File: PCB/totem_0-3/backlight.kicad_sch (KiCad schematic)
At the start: 40 parts

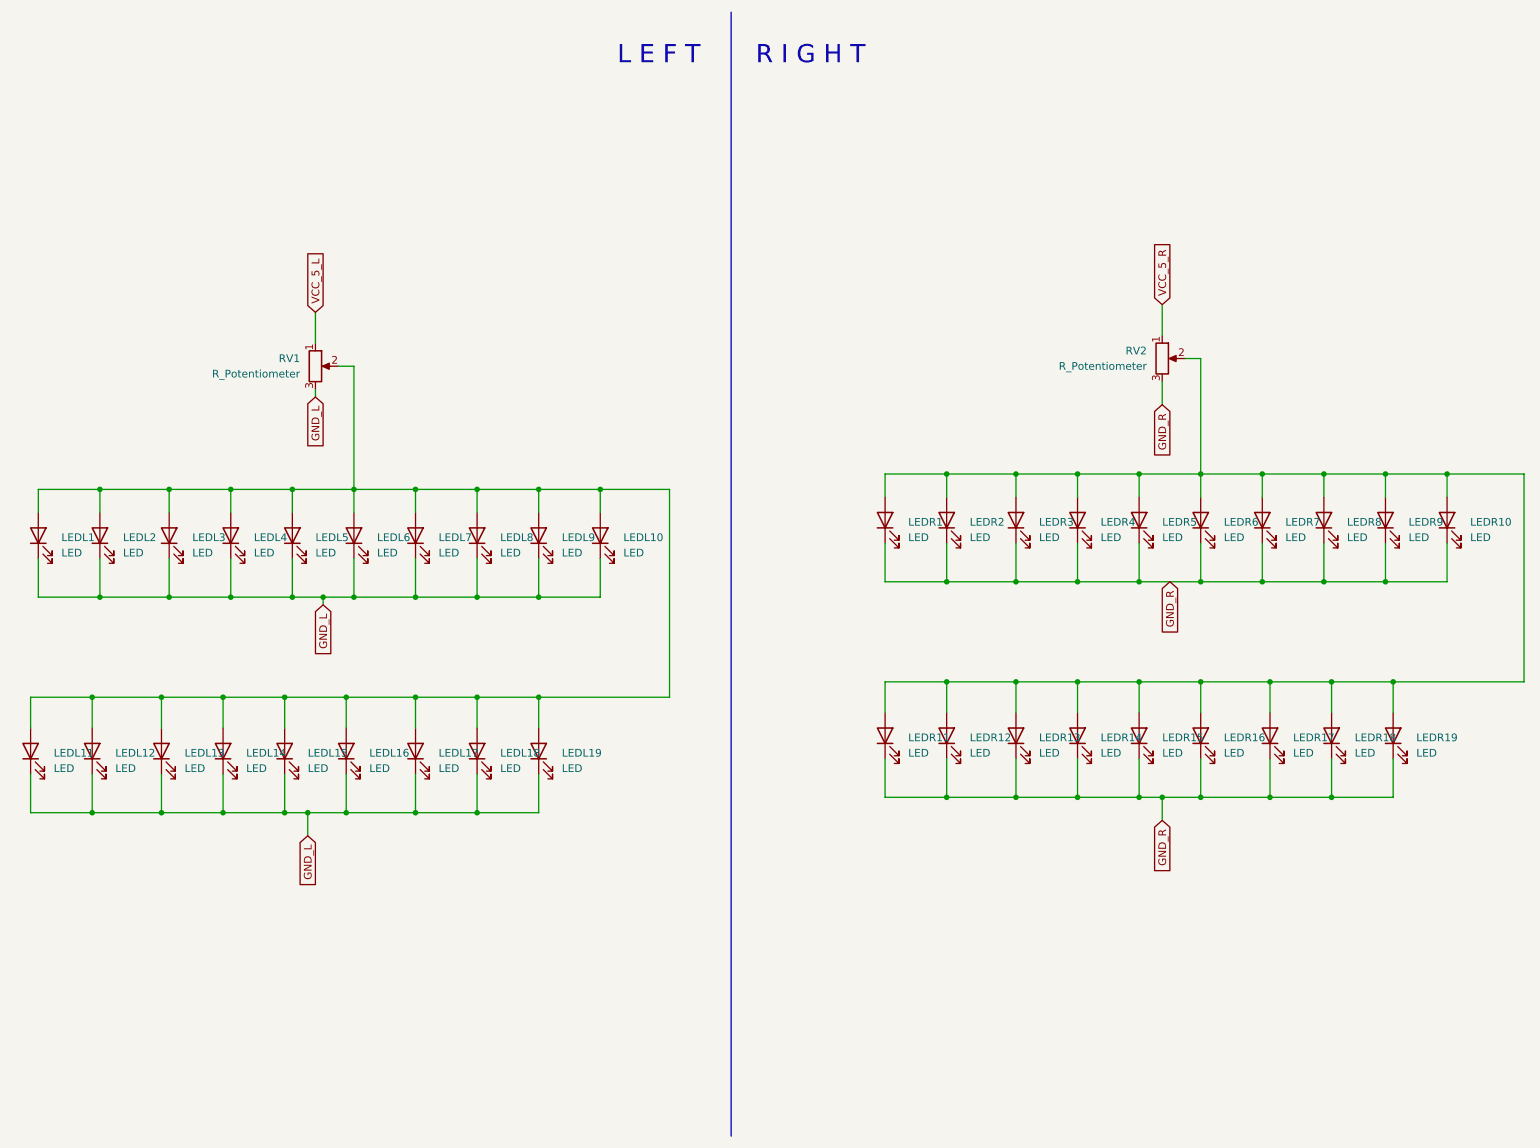
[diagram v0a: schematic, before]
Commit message: updated backlight shematics with new leds, default led uses reversed pin number assigns, aka : leds get mounted backwards by pick and place, what a tragedy
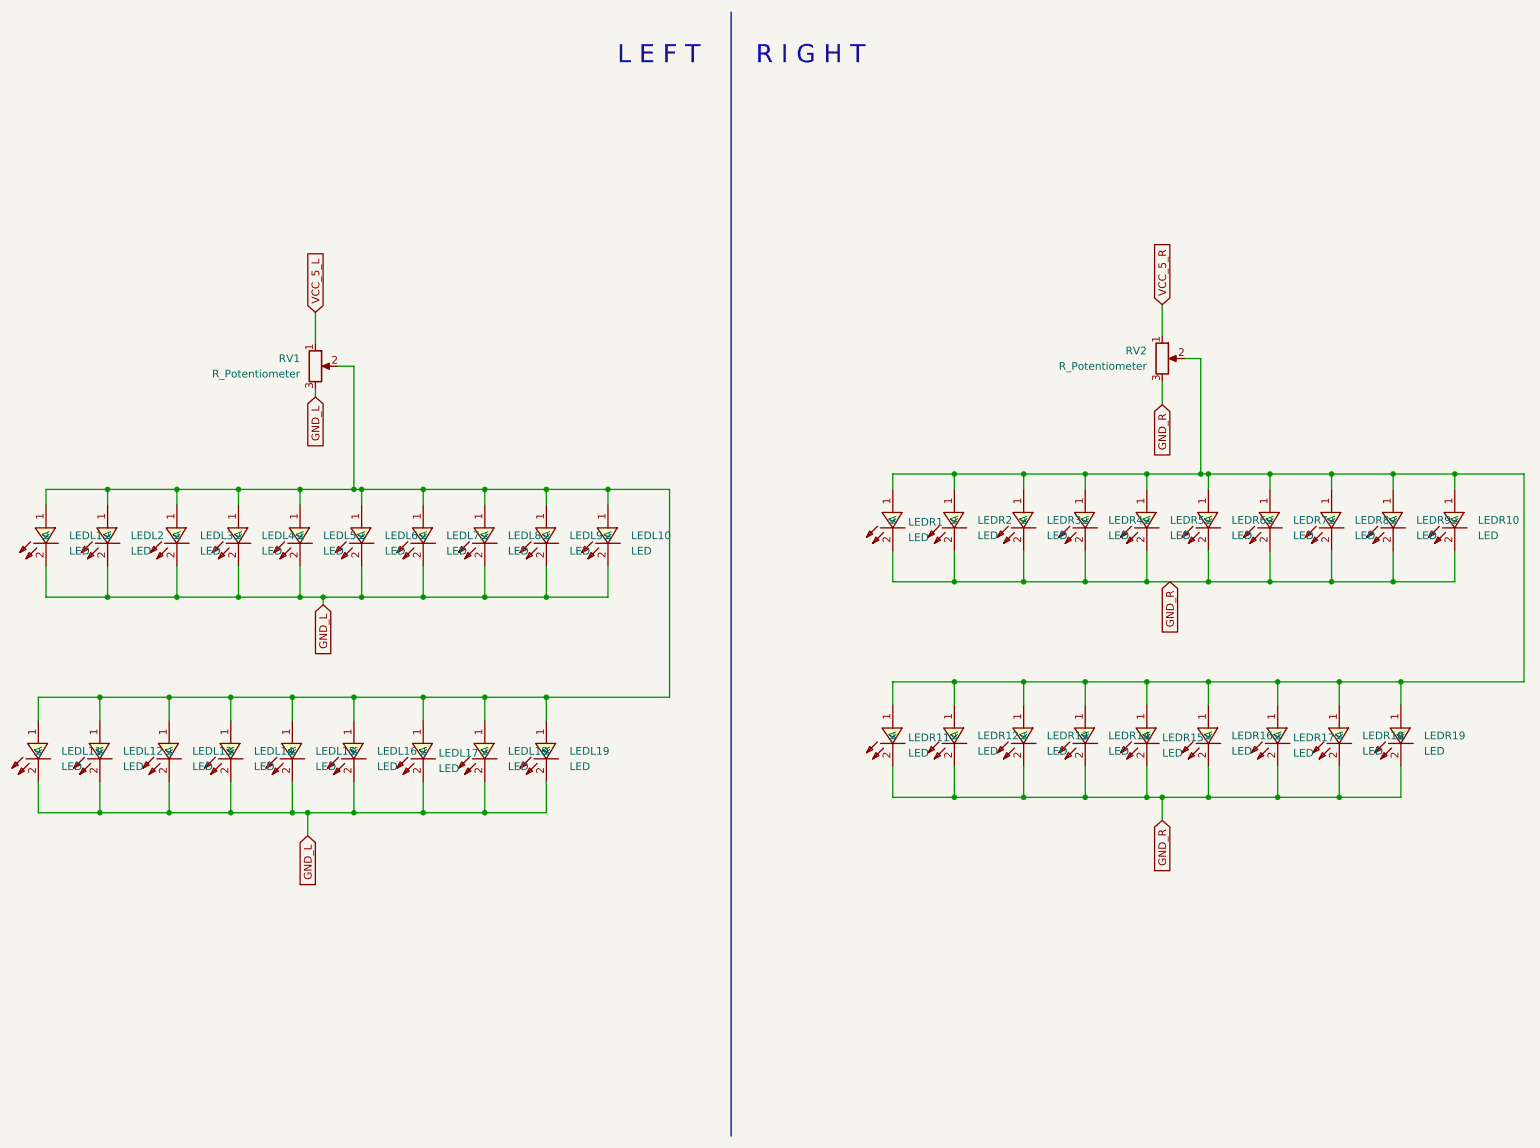
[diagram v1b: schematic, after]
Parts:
- LEDL1, LEDL10, LEDL11, LEDL12, LEDL13, LEDL14, LEDL15, LEDL16, LEDL17, LEDL18, LEDL19, LEDL2, LEDL3, LEDL4, LEDL5, LEDL6, LEDL7, LEDL8, LEDL9, LEDR1, LEDR10, LEDR11, LEDR12, LEDR13, LEDR14, LEDR15, LEDR16, LEDR17, LEDR18, LEDR19, LEDR2, LEDR3, LEDR4, LEDR5, LEDR6, LEDR7, LEDR8, LEDR9: symbol Device:LED -> Totem_lib:0603Whitelight_C2290; LCSC Part (none) -> C2290
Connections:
- net GND_L: now also LEDL1.2 (K), LEDL10.2 (K), LEDL11.2 (K), LEDL12.2 (K), LEDL13.2 (K), LEDL14.2 (K), LEDL15.2 (K), LEDL16.2 (K), LEDL17.2 (K), LEDL18.2 (K), LEDL19.2 (K), LEDL2.2 (K), LEDL3.2 (K), LEDL4.2 (K), LEDL5.2 (K), LEDL6.2 (K), LEDL7.2 (K), LEDL8.2 (K), LEDL9.2 (K); no longer LEDL1.1 (K), LEDL10.1 (K), LEDL11.1 (K), LEDL12.1 (K), LEDL13.1 (K), LEDL14.1 (K), LEDL15.1 (K), LEDL16.1 (K), LEDL17.1 (K), LEDL18.1 (K), LEDL19.1 (K), LEDL2.1 (K), LEDL3.1 (K), LEDL4.1 (K), LEDL5.1 (K), LEDL6.1 (K), LEDL7.1 (K), LEDL8.1 (K), LEDL9.1 (K)
- net GND_R: now also LEDR1.2 (K), LEDR10.2 (K), LEDR11.2 (K), LEDR12.2 (K), LEDR13.2 (K), LEDR14.2 (K), LEDR15.2 (K), LEDR16.2 (K), LEDR17.2 (K), LEDR18.2 (K), LEDR19.2 (K), LEDR2.2 (K), LEDR3.2 (K), LEDR4.2 (K), LEDR5.2 (K), LEDR6.2 (K), LEDR7.2 (K), LEDR8.2 (K), LEDR9.2 (K); no longer LEDR1.1 (K), LEDR10.1 (K), LEDR11.1 (K), LEDR12.1 (K), LEDR13.1 (K), LEDR14.1 (K), LEDR15.1 (K), LEDR16.1 (K), LEDR17.1 (K), LEDR18.1 (K), LEDR19.1 (K), LEDR2.1 (K), LEDR3.1 (K), LEDR4.1 (K), LEDR5.1 (K), LEDR6.1 (K), LEDR7.1 (K), LEDR8.1 (K), LEDR9.1 (K)
- new net: LEDL1.1 (A), LEDL10.1 (A), LEDL11.1 (A), LEDL12.1 (A), LEDL13.1 (A), LEDL14.1 (A), LEDL15.1 (A), LEDL16.1 (A), LEDL17.1 (A), LEDL18.1 (A), LEDL19.1 (A), LEDL2.1 (A), LEDL3.1 (A), LEDL4.1 (A), LEDL5.1 (A), LEDL6.1 (A), LEDL7.1 (A), LEDL8.1 (A), LEDL9.1 (A), RV1.2
- new net: LEDR1.1 (A), LEDR10.1 (A), LEDR11.1 (A), LEDR12.1 (A), LEDR13.1 (A), LEDR14.1 (A), LEDR15.1 (A), LEDR16.1 (A), LEDR17.1 (A), LEDR18.1 (A), LEDR19.1 (A), LEDR2.1 (A), LEDR3.1 (A), LEDR4.1 (A), LEDR5.1 (A), LEDR6.1 (A), LEDR7.1 (A), LEDR8.1 (A), LEDR9.1 (A), RV2.2
